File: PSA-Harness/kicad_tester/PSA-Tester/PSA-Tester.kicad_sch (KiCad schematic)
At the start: 35 parts, among them J11 USB_C_Receptacle, SW1 SW_Push, SW2 SW_Push, SW3 SW_Push, U1 MCP23017_SO, U10 ESP32-C3-OLED, U2 MCP23017_SO, U3 MCP23017_SO, U4 MCP23017_SO, U5 MCP23017_SO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

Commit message: swap mux footprint to DIP-28
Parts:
- J11: footprint Connector_USB:USB_C_Receptacle_Molex_105450-0101 -> 0_tester:TYPE-C-31-M-04
- U1, U2, U3, U4, U5, U6, U7, U8, U9: footprint Package_SO:SOIC-28W_7.5x17.9mm_P1.27mm -> Package_DIP:CERDIP-28_W7.62mm_SideBrazed_LongPads
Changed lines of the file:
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@@
 			)
 		)
-		(property "Footprint" "Package_SO:SOIC-28W_7.5x17.9mm_P1.27mm"
+		(property "Footprint" "Package_DIP:CERDIP-28_W7.62mm_SideBrazed_LongPads"
 			(at 163.83 195.58 0)
 			(effects
@@
 			)
 		)
-		(property "Footprint" "Package_SO:SOIC-28W_7.5x17.9mm_P1.27mm"
+		(property "Footprint" "Package_DIP:CERDIP-28_W7.62mm_SideBrazed_LongPads"
 			(at 220.98 269.24 0)
 			(effects
@@
 			)
 		)
-		(property "Footprint" "Package_SO:SOIC-28W_7.5x17.9mm_P1.27mm"
+		(property "Footprint" "Package_DIP:CERDIP-28_W7.62mm_SideBrazed_LongPads"
 			(at 220.98 195.58 0)
 			(effects
@@
 			)
 		)
-		(property "Footprint" "Package_SO:SOIC-28W_7.5x17.9mm_P1.27mm"
+		(property "Footprint" "Package_DIP:CERDIP-28_W7.62mm_SideBrazed_LongPads"
 			(at 163.83 269.24 0)
 			(effects
@@
 			)
 		)
-		(property "Footprint" "Package_SO:SOIC-28W_7.5x17.9mm_P1.27mm"
+		(property "Footprint" "Package_DIP:CERDIP-28_W7.62mm_SideBrazed_LongPads"
 			(at 106.68 269.24 0)
 			(effects
@@
 			)
 		)
-		(property "Footprint" "Package_SO:SOIC-28W_7.5x17.9mm_P1.27mm"
+		(property "Footprint" "Package_DIP:CERDIP-28_W7.62mm_SideBrazed_LongPads"
 			(at 49.53 195.58 0)
 			(effects
@@
 			)
 		)
-		(property "Footprint" "Package_SO:SOIC-28W_7.5x17.9mm_P1.27mm"
+		(property "Footprint" "Package_DIP:CERDIP-28_W7.62mm_SideBrazed_LongPads"
 			(at 49.53 269.24 0)
 			(effects
@@
 			)
 		)
-		(property "Footprint" "Package_SO:SOIC-28W_7.5x17.9mm_P1.27mm"
+		(property "Footprint" "Package_DIP:CERDIP-28_W7.62mm_SideBrazed_LongPads"
 			(at 275.59 269.24 0)
 			(effects
@@
 			)
 		)
-		(property "Footprint" "Package_SO:SOIC-28W_7.5x17.9mm_P1.27mm"
+		(property "Footprint" "Package_DIP:CERDIP-28_W7.62mm_SideBrazed_LongPads"
 			(at 106.68 195.58 0)
 			(effects
@@
 			)
 		)
-		(property "Footprint" "Connector_USB:USB_C_Receptacle_Molex_105450-0101"
+		(property "Footprint" "0_tester:TYPE-C-31-M-04"
 			(at 259.08 80.01 0)
 			(effects

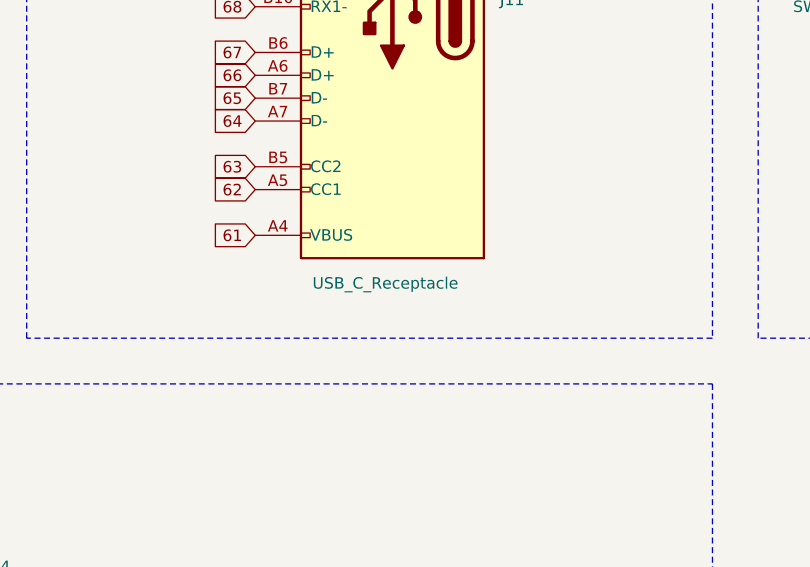
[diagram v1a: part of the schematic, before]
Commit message: routed with SMD packages
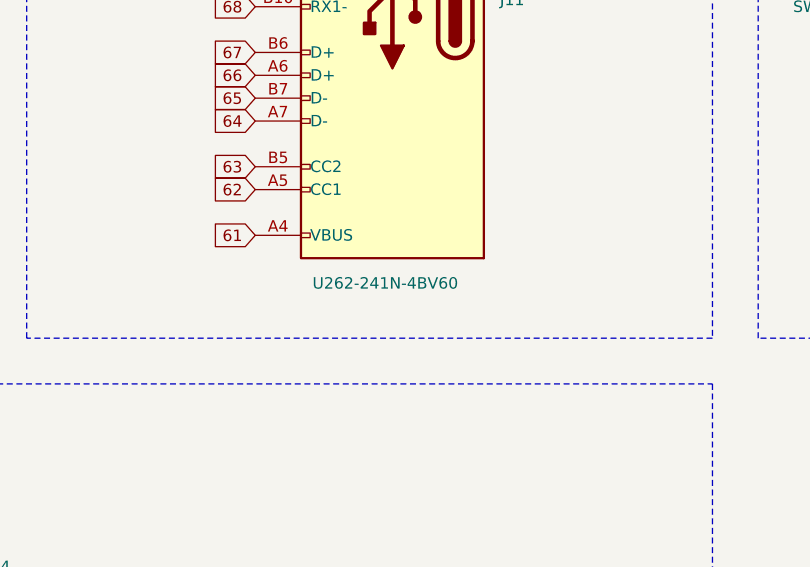
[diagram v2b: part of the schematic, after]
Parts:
- J11: value USB_C_Receptacle -> U262-241N-4BV60
- SW1, SW2, SW3: value SW_Push -> B3S-1000
- U1, U2, U3, U4, U5, U6, U7, U8, U9: footprint Package_DIP:CERDIP-28_W7.62mm_SideBrazed_LongPads -> Package_SO:SOIC-28W_7.5x18.7mm_P1.27mm
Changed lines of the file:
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@@
 			)
 		)
-		(property "Footprint" "Package_DIP:CERDIP-28_W7.62mm_SideBrazed_LongPads"
+		(property "Footprint" "Package_SO:SOIC-28W_7.5x18.7mm_P1.27mm"
 			(at 163.83 195.58 0)
 			(effects
@@
 			)
 		)
-		(property "Value" "SW_Push"
+		(property "Value" "B3S-1000"
 			(at 310.642 80.01 0)
 			(effects
@@
 			)
 		)
-		(property "Footprint" "Package_DIP:CERDIP-28_W7.62mm_SideBrazed_LongPads"
+		(property "Footprint" "Package_SO:SOIC-28W_7.5x18.7mm_P1.27mm"
 			(at 220.98 269.24 0)
 			(effects
@@
 			)
 		)
-		(property "Footprint" "Package_DIP:CERDIP-28_W7.62mm_SideBrazed_LongPads"
+		(property "Footprint" "Package_SO:SOIC-28W_7.5x18.7mm_P1.27mm"
 			(at 220.98 195.58 0)
 			(effects
@@
 			)
 		)
-		(property "Footprint" "Package_DIP:CERDIP-28_W7.62mm_SideBrazed_LongPads"
+		(property "Footprint" "Package_SO:SOIC-28W_7.5x18.7mm_P1.27mm"
 			(at 163.83 269.24 0)
 			(effects
@@
 			)
 		)
-		(property "Footprint" "Package_DIP:CERDIP-28_W7.62mm_SideBrazed_LongPads"
+		(property "Footprint" "Package_SO:SOIC-28W_7.5x18.7mm_P1.27mm"
 			(at 106.68 269.24 0)
 			(effects
@@
 			)
 		)
-		(property "Footprint" "Package_DIP:CERDIP-28_W7.62mm_SideBrazed_LongPads"
+		(property "Footprint" "Package_SO:SOIC-28W_7.5x18.7mm_P1.27mm"
 			(at 49.53 195.58 0)
 			(effects
@@
 			)
 		)
-		(property "Footprint" "Package_DIP:CERDIP-28_W7.62mm_SideBrazed_LongPads"
+		(property "Footprint" "Package_SO:SOIC-28W_7.5x18.7mm_P1.27mm"
 			(at 49.53 269.24 0)
 			(effects
@@
 			)
 		)
-		(property "Value" "SW_Push"
+		(property "Value" "B3S-1000"
 			(at 370.332 80.01 0)
 			(effects
@@
 			)
 		)
-		(property "Footprint" "Package_DIP:CERDIP-28_W7.62mm_SideBrazed_LongPads"
+		(property "Footprint" "Package_SO:SOIC-28W_7.5x18.7mm_P1.27mm"
 			(at 275.59 269.24 0)
 			(effects
@@
 			)
 		)
-		(property "Footprint" "Package_DIP:CERDIP-28_W7.62mm_SideBrazed_LongPads"
+		(property "Footprint" "Package_SO:SOIC-28W_7.5x18.7mm_P1.27mm"
 			(at 106.68 195.58 0)
 			(effects
@@
 			)
 		)
-		(property "Value" "SW_Push"
+		(property "Value" "B3S-1000"
 			(at 341.122 80.01 0)
 			(effects
@@
 			)
 		)
-		(property "Value" "USB_C_Receptacle"
+		(property "Value" "U262-241N-4BV60"
 			(at 254 110.744 0)
 			(effects

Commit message: part fixes
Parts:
- SW1, SW2, SW3: footprint Button_Switch_SMD:SW_SPST_B3S-1000 -> 0_tester:SW_SPST_B3S-1000
- U1, U2, U3, U4, U5, U6, U7, U8, U9: value MCP23017_SO -> MCP23017T-E/SO
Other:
- note added: "OBD-C"
- note removed: "OBC-C"
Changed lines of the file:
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@@
 		)
 	)
-	(text "OBC-C"
+	(text "OBD-C"
 		(exclude_from_sim no)
 		(at 259.08 25.146 0)
@@
 			)
 		)
-		(property "Value" "MCP23017_SO"
+		(property "Value" "MCP23017T-E/SO"
 			(at 160.8933 144.78 0)
 			(effects
@@
 			)
 		)
-		(property "Footprint" "Button_Switch_SMD:SW_SPST_B3S-1000"
+		(property "Footprint" "0_tester:SW_SPST_B3S-1000"
 			(at 309.88 80.01 0)
 			(effects
@@
 			)
 		)
-		(property "Value" "MCP23017_SO"
+		(property "Value" "MCP23017T-E/SO"
 			(at 218.0433 218.44 0)
 			(effects
@@
 			)
 		)
-		(property "Value" "MCP23017_SO"
+		(property "Value" "MCP23017T-E/SO"
 			(at 218.0433 144.78 0)
 			(effects
@@
 			)
 		)
-		(property "Value" "MCP23017_SO"
+		(property "Value" "MCP23017T-E/SO"
 			(at 160.8933 218.44 0)
 			(effects
@@
 			)
 		)
-		(property "Value" "MCP23017_SO"
+		(property "Value" "MCP23017T-E/SO"
 			(at 103.7433 218.44 0)
 			(effects
@@
 			)
 		)
-		(property "Value" "MCP23017_SO"
+		(property "Value" "MCP23017T-E/SO"
 			(at 46.5933 144.78 0)
 			(effects
@@
 			)
 		)
-		(property "Value" "MCP23017_SO"
+		(property "Value" "MCP23017T-E/SO"
 			(at 46.5933 218.44 0)
 			(effects
@@
 			)
 		)
-		(property "Footprint" "Button_Switch_SMD:SW_SPST_B3S-1000"
+		(property "Footprint" "0_tester:SW_SPST_B3S-1000"
 			(at 369.57 80.01 0)
 			(effects
@@
 			)
 		)
-		(property "Value" "MCP23017_SO"
+		(property "Value" "MCP23017T-E/SO"
 			(at 272.6533 218.44 0)
 			(effects
@@
 			)
 		)
-		(property "Value" "MCP23017_SO"
+		(property "Value" "MCP23017T-E/SO"
 			(at 103.7433 144.78 0)
 			(effects
@@
 			)
 		)
-		(property "Footprint" "Button_Switch_SMD:SW_SPST_B3S-1000"
+		(property "Footprint" "0_tester:SW_SPST_B3S-1000"
 			(at 340.36 80.01 0)
 			(effects

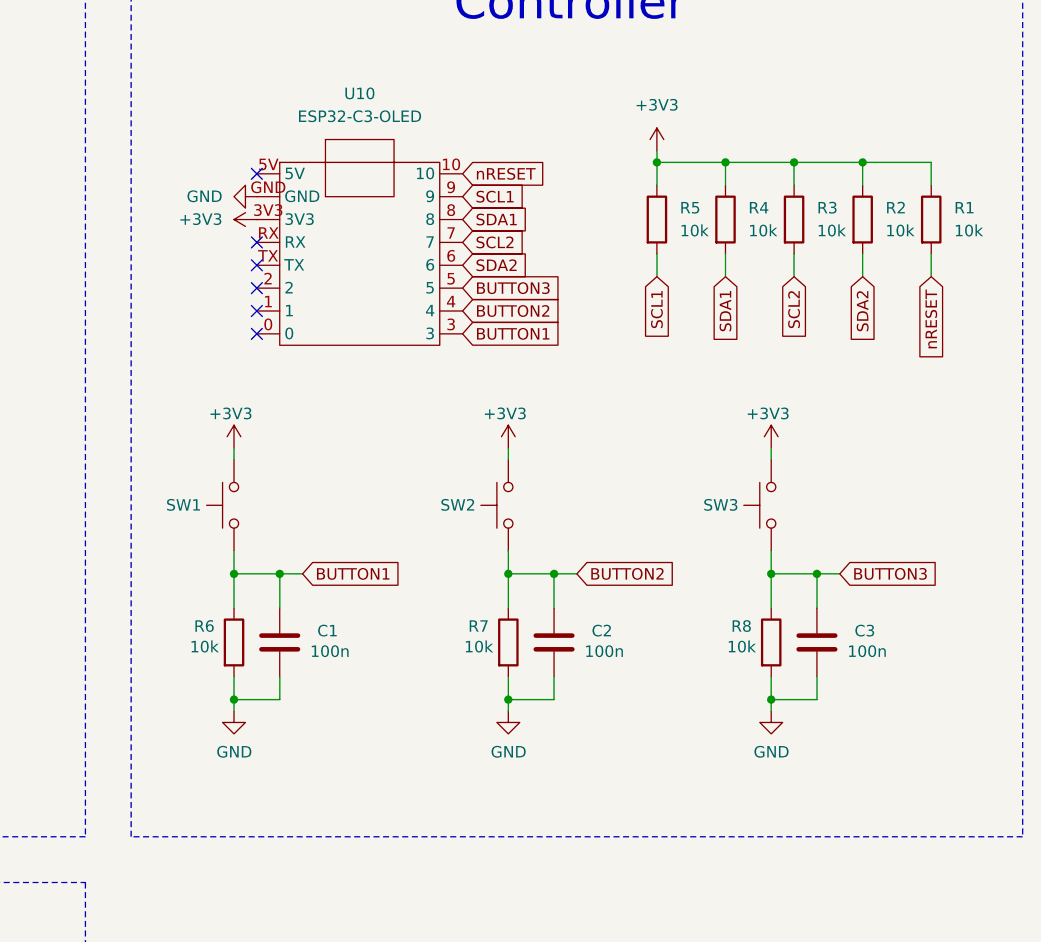
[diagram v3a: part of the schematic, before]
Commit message: add RGB LED
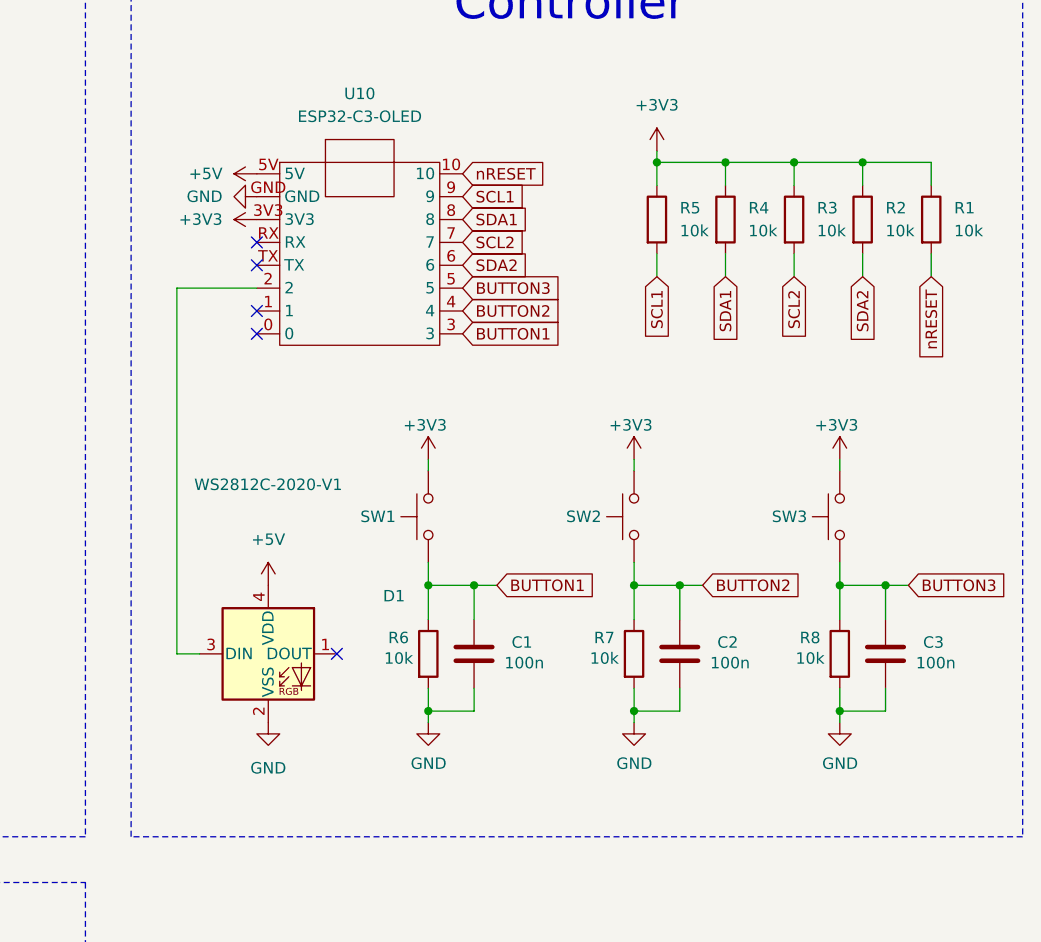
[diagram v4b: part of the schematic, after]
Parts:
- added D1: WS2812C-2020-V1, 0_tester:LED_WS2812B-2020_PLCC4_2.0x2.0mm, symbol LED:WS2812B-2020
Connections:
- net GND: now also D1.2 (VSS)
- net at U10.2: now also D1.3 (DIN)
- net +5V: now reaches U10.5V
- net +5V: now also D1.4 (VDD)
- no-connect marks 29 -> 28
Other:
- moved on the sheet: C1, C2, C3, R6, R7, R8, SW1, SW2, SW3

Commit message: add texts
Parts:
- added C4: 10u, Capacitor_SMD:C_1206_3216Metric_Pad1.33x1.80mm_HandSolder, symbol Device:C
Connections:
- net +3V3: now also C4.1
- net GND: now also C4.2
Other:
- moved on the sheet: R1, R2, R3, R4, R5

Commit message: routed
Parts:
- D1: value WS2812C-2020-V1 -> XL-0807RGBC-WS2812B
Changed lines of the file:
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@@
 			)
 		)
-		(property "Value" "WS2812C-2020-V1"
+		(property "Value" "XL-0807RGBC-WS2812B"
 			(at 318.77 77.724 0)
 			(effects

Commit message: change usb-c type and button
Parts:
- J11: value U262-241N-4BV60 -> TYPE-C-31-M-04
- SW1, SW2, SW3: value B3S-1000 -> B3FS-1010P; footprint 0_tester:SW_SPST_B3S-1000 -> 0_tester:SW_SPST_Omron_B3FS-101xP
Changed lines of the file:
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@@
 			)
 		)
-		(property "Value" "B3S-1000"
+		(property "Value" "B3FS-1010P"
 			(at 332.232 81.28 0)
 			(effects
@@
 			)
 		)
-		(property "Footprint" "0_tester:SW_SPST_B3S-1000"
+		(property "Footprint" "0_tester:SW_SPST_Omron_B3FS-101xP"
 			(at 331.47 81.28 0)
 			(effects
@@
 			)
 		)
-		(property "Value" "B3S-1000"
+		(property "Value" "B3FS-1010P"
 			(at 377.952 81.28 0)
 			(effects
@@
 			)
 		)
-		(property "Footprint" "0_tester:SW_SPST_B3S-1000"
+		(property "Footprint" "0_tester:SW_SPST_Omron_B3FS-101xP"
 			(at 377.19 81.28 0)
 			(effects
@@
 			)
 		)
-		(property "Value" "B3S-1000"
+		(property "Value" "B3FS-1010P"
 			(at 355.092 81.28 0)
 			(effects
@@
 			)
 		)
-		(property "Footprint" "0_tester:SW_SPST_B3S-1000"
+		(property "Footprint" "0_tester:SW_SPST_Omron_B3FS-101xP"
 			(at 354.33 81.28 0)
 			(effects
@@
 			)
 		)
-		(property "Value" "U262-241N-4BV60"
+		(property "Value" "TYPE-C-31-M-04"
 			(at 254 110.744 0)
 			(effects

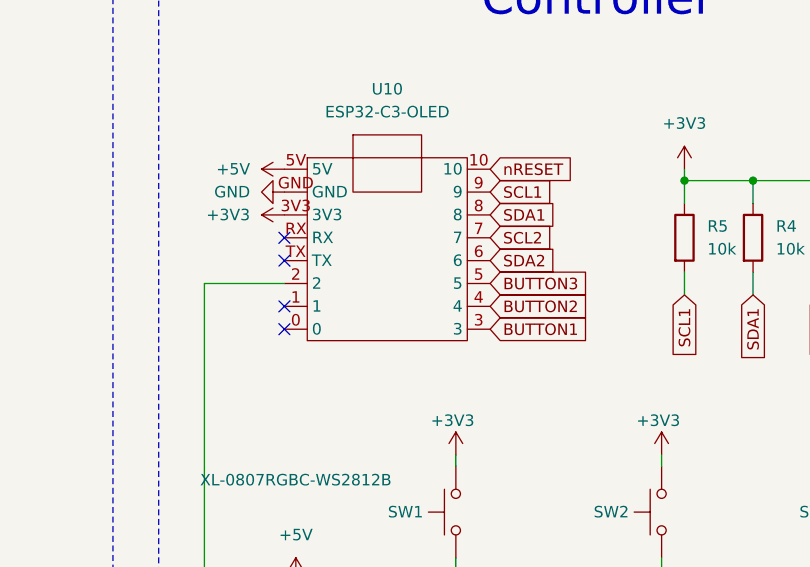
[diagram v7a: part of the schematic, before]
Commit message: fix pin5/pin6 used by I2C OLED
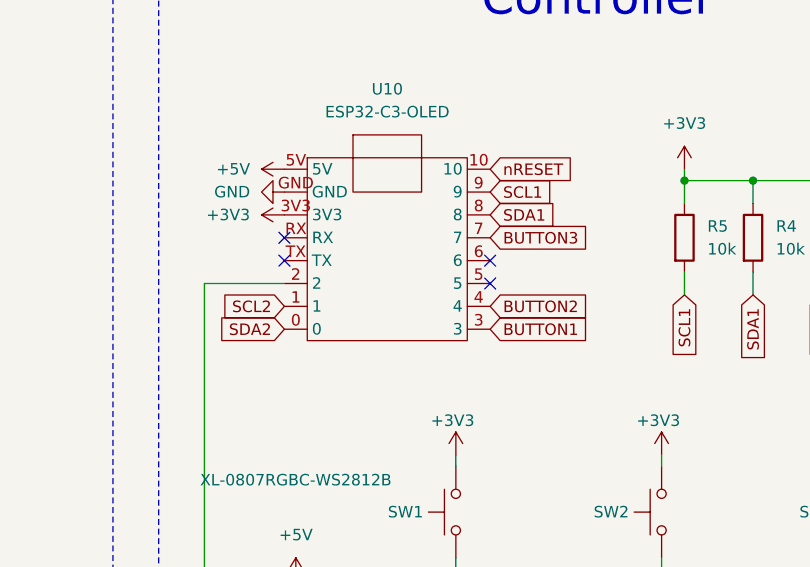
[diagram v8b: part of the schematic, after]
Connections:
- net BUTTON3: now also U10.7; no longer U10.5
- net SCL2: now also U10.1; no longer U10.7
- net SDA2: now also U10.0; no longer U10.6
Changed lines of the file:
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@@
 	)
 	(no_connect
+		(at 340.36 55.88)
+	)
+	(no_connect
 		(at 233.68 185.42)
 	)
@@
 	)
 	(no_connect
-		(at 252.73 238.76)
+		(at 340.36 53.34)
 	)
 	(no_connect
-		(at 317.5 58.42)
+		(at 252.73 238.76)
 	)
 	(no_connect
@@
 	)
 	(no_connect
-		(at 317.5 60.96)
-	)
-	(no_connect
 		(at 317.5 53.34)
 	)
@@
 	(global_label "BUTTON3"
 		(shape input)
-		(at 340.36 55.88 0)
+		(at 340.36 50.8 0)
 		(fields_autoplaced yes)
 		(effects
@@
 		)
 		(property "Intersheetrefs" "${INTERSHEET_REFS}"
-			(at 351.7514 55.88 0)
+			(at 351.7514 50.8 0)
 			(effects
 				(font
@@
 		)
 	)
+	(global_label "SCL2"
+		(shape input)
+		(at 317.5 58.42 180)
+		(fields_autoplaced yes)
+		(effects
+			(font
+				(size 1.27 1.27)
+			)
+			(justify right)
+		)
+		(property "Intersheetrefs" "${INTERSHEET_REFS}"
+			(at 309.7977 58.42 0)
+			(effects
+				(font
+					(size 1.27 1.27)
+				)
+				(justify right)
+				(hide yes)
+			)
+		)
+	)
 	(global_label "48a"
 		(shape input)
@@
 		)
 	)
-	(global_label "SDA2"
-		(shape input)
-		(at 340.36 53.34 0)
-		(fields_autoplaced yes)
-		(effects
-			(font
-				(size 1.27 1.27)
-			)
-			(justify left)
-		)
-		(property "Intersheetrefs" "${INTERSHEET_REFS}"
-			(at 348.1228 53.34 0)
-			(effects
-				(font
-					(size 1.27 1.27)
-				)
-				(justify left)
-				(hide yes)
-			)
-		)
-	)
 	(global_label "74"
 		(shape input)
@@
 		)
 	)
-	(global_label "SCL2"
-		(shape input)
-		(at 340.36 50.8 0)
-		(fields_autoplaced yes)
-		(effects
-			(font
-				(size 1.27 1.27)
-			)
-			(justify left)
-		)
-		(property "Intersheetrefs" "${INTERSHEET_REFS}"
-			(at 348.0623 50.8 0)
-			(effects
-				(font
-					(size 1.27 1.27)
-				)
-				(justify left)
-				(hide yes)
-			)
-		)
-	)
 	(global_label "18"
 		(shape input)
@@
 			(effects
 				(font
+					(size 1.27 1.27)
+				)
+				(justify right)
+				(hide yes)
+			)
+		)
+	)
+	(global_label "SDA2"
+		(shape input)
+		(at 317.5 60.96 180)
+		(fields_autoplaced yes)
+		(effects
+			(font
+				(size 1.27 1.27)
+			)
+			(justify right)
+		)
+		(property "Intersheetrefs" "${INTERSHEET_REFS}"
+			(at 309.7372 60.96 0)
+			(effects
+				(font
